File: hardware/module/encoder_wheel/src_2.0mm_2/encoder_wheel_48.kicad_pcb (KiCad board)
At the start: 2 copper layers, 74 x 74 mm, 2 parts

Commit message: encoder changes
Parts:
- renumbered REF** to ENC1, REF** to ENC2

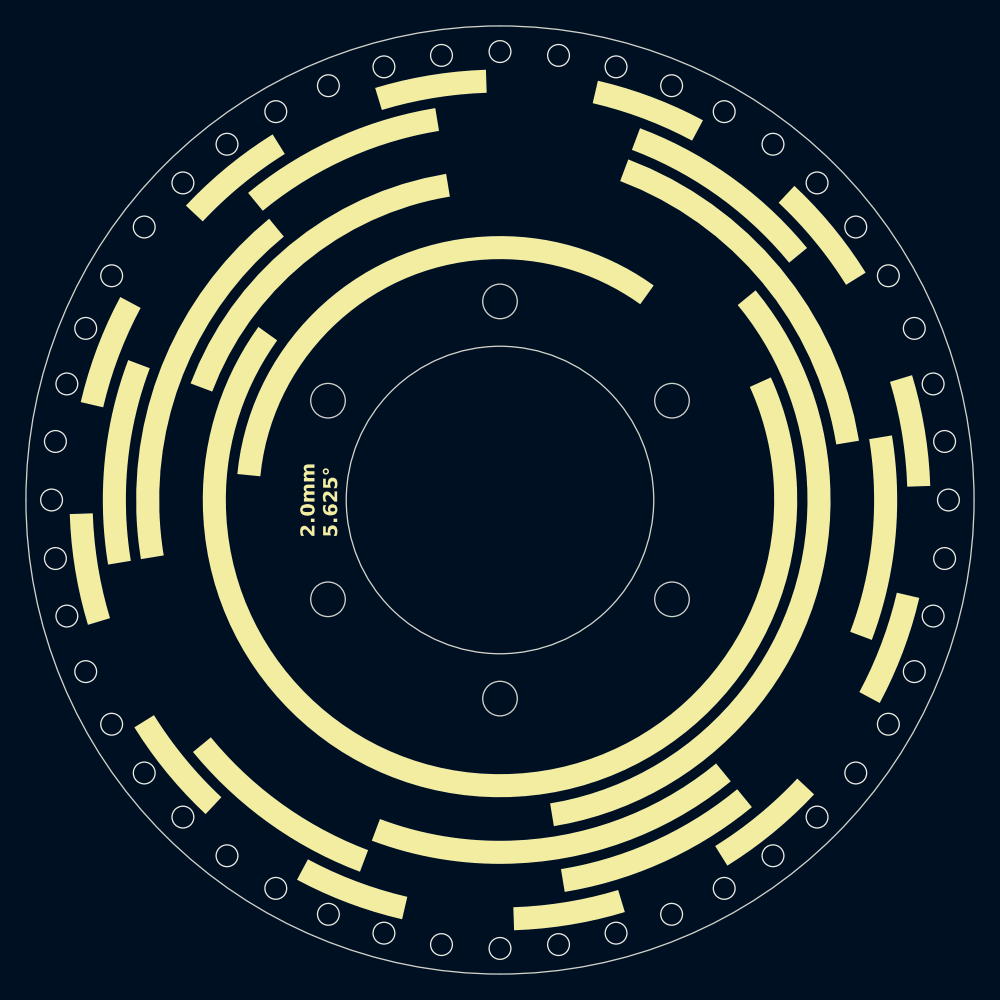
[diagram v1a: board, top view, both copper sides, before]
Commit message: changed hole patern encoder wheel
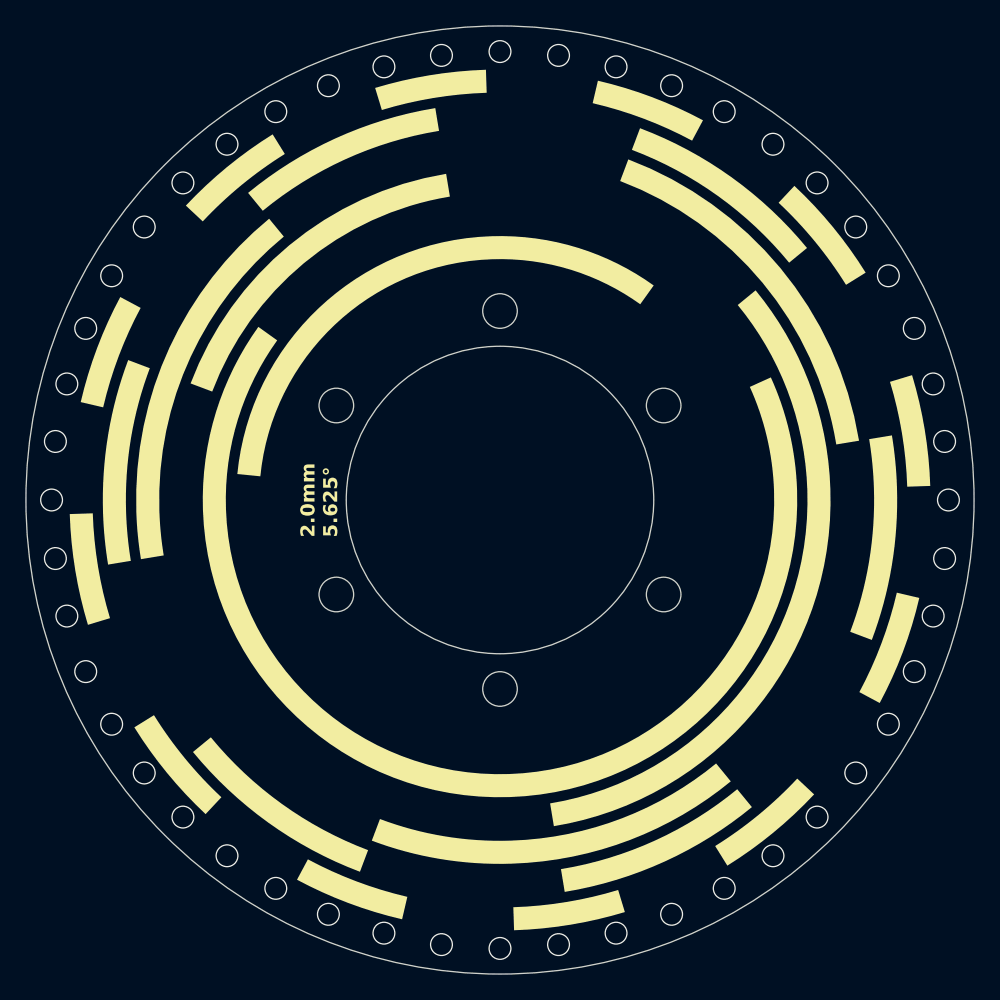
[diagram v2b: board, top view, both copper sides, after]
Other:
- outline, holes or cut-outs redrawn
